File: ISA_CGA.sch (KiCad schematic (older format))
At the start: 0 parts

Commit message: Complete a sheet
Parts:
- added U13: 74LS08, Package_DIP:DIP-14_W7.62mm_LongPads, symbol 74xx:74LS08
- added U14: 74LS32, Package_DIP:DIP-14_W7.62mm_LongPads, symbol 74xx:74LS32
- added U28: 74LS10, Package_DIP:DIP-14_W7.62mm_LongPads, symbol 74xx:74LS10
- added U48: 74LS51, Package_DIP:DIP-14_W7.62mm_LongPads, symbol 74xx:74LS51
- added U49: 74LS02, symbol 74xx:74LS02
- added U62: 74LS125, Package_DIP:DIP-14_W10.16mm_LongPads, symbol 74xx:74LS125
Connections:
- new net GND: U13.14 (VCC), U14.14 (VCC), U28.7 (GND), U48.7 (GND), U49.7 (GND), U62.7 (GND)
- new net VCC: U13.7 (GND), U14.7 (GND), U28.14 (VCC), U48.14 (VCC), U49.14 (VCC), U62.14 (VCC)
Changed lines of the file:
@@
 F1 "CGA_6_6.sch" 50
 $EndSheet
+$Comp
+L 74xx:74LS51 U?
+U 3 1 604901DC
+P 3000 4850
+AR Path="/60463BAE/604901DC" Ref="U?"  Part="1"
+AR Path="/604901DC" Ref="U48"  Part="3"
+F 0 "U48" H 2850 5200 50  0000 C CNN
+F 1 "74LS51" H 3150 5200 50  0000 C CNN
+F 2 "Package_DIP:DIP-14_W7.62mm_LongPads" H 3000 4850 50  0001 C CNN
+F 3 "http://www.ti.com/lit/ds/symlink/sn74ls51.pdf" H 3000 4850 50  0001 C CNN
+	3    3000 4850
+	1    0    0    -1
+$EndComp
+$Comp
+L power:GND #PWR?
+U 1 1 60491E97
+P 3000 5350
+F 0 "#PWR?" H 3000 5100 50  0001 C CNN
+F 1 "GND" H 3005 5177 50  0000 C CNN
+F 2 "" H 3000 5350 50  0001 C CNN
+F 3 "" H 3000 5350 50  0001 C CNN
+	1    3000 5350
+	1    0    0    -1
+$EndComp
+$Comp
+L power:VCC #PWR?
+U 1 1 604924E0
+P 3000 4350
+F 0 "#PWR?" H 3000 4200 50  0001 C CNN
+F 1 "VCC" H 3015 4523 50  0000 C CNN
+F 2 "" H 3000 4350 50  0001 C CNN
+F 3 "" H 3000 4350 50  0001 C CNN
+	1    3000 4350
+	1    0    0    -1
+$EndComp
+$Comp
+L 74xx:74LS02 U?
+U 5 1 60495092
+P 3600 4850
+AR Path="/60463BAE/60495092" Ref="U?"  Part="3"
+AR Path="/60495092" Ref="U49"  Part="5"
+F 0 "U49" H 3500 5200 50  0000 C CNN
+F 1 "74LS02" H 3750 5200 50  0000 C CNN
+F 2 "" H 3600 4850 50  0001 C CNN
+F 3 "http://www.ti.com/lit/gpn/sn74ls02" H 3600 4850 50  0001 C CNN
+	5    3600 4850
+	1    0    0    -1
+$EndComp
+Connection ~ 3000 4350
+Connection ~ 3000 5350
+$Comp
+L 74xx:74LS125 U?
+U 5 1 6049EC67
+P 4200 4850
+AR Path="/60463BAE/6049EC67" Ref="U?"  Part="1"
+AR Path="/6049EC67" Ref="U62"  Part="5"
+F 0 "U62" H 4050 5200 50  0000 C CNN
+F 1 "74LS125" H 4400 5200 50  0000 C CNN
+F 2 "Package_DIP:DIP-14_W10.16mm_LongPads" H 4200 4850 50  0001 C CNN
+F 3 "http://www.ti.com/lit/gpn/sn74LS125" H 4200 4850 50  0001 C CNN
+	5    4200 4850
+	1    0    0    -1
+$EndComp
+Connection ~ 3600 4350
+Connection ~ 3600 5350
+Wire Wire Line
+	3000 4350 3600 4350
+Wire Wire Line
+	3000 5350 3600 5350
+Wire Wire Line
+	3600 4350 4200 4350
+Wire Wire Line
+	3600 5350 4200 5350
+$Comp
+L 74xx:74LS08 U?
+U 5 1 60735FFE
+P 1200 4850
+AR Path="/60463BAE/60735FFE" Ref="U?"  Part="4"
+AR Path="/60735FFE" Ref="U13"  Part="5"
+F 0 "U13" H 1150 4500 50  0000 R CNN
+F 1 "74LS08" H 1500 4500 50  0000 R CNN
+F 2 "Package_DIP:DIP-14_W7.62mm_LongPads" H 1200 4850 50  0001 C CNN
+F 3 "http://www.ti.com/lit/gpn/sn74LS08" H 1200 4850 50  0001 C CNN
+	5    1200 4850
+	1    0    0    1
+$EndComp
+$Comp
+L 74xx:74LS10 U?
+U 4 1 6073B547
+P 2400 4850
+AR Path="/60463BAE/6073B547" Ref="U?"  Part="3"
+AR Path="/6073B547" Ref="U28"  Part="4"
+F 0 "U28" H 2150 5200 50  0000 L CNN
+F 1 "74LS10" H 2450 5200 50  0000 L CNN
+F 2 "Package_DIP:DIP-14_W7.62mm_LongPads" H 2400 4850 50  0001 C CNN
+F 3 "http://www.ti.com/lit/gpn/sn74LS10" H 2400 4850 50  0001 C CNN
+	4    2400 4850
+	1    0    0    -1
+$EndComp
+$Comp
+L 74xx:74LS32 U?
+U 5 1 607513C2
+P 1800 4850
+AR Path="/60463BAE/607513C2" Ref="U?"  Part="2"
+AR Path="/607513C2" Ref="U14"  Part="5"
+F 0 "U14" H 1750 4500 50  0000 R CNN
+F 1 "74LS32" H 2100 4500 50  0000 R CNN
+F 2 "Package_DIP:DIP-14_W7.62mm_LongPads" H 1800 4850 50  0001 C CNN
+F 3 "http://www.ti.com/lit/gpn/sn74LS32" H 1800 4850 50  0001 C CNN
+	5    1800 4850
+	1    0    0    1
+$EndComp
+Wire Wire Line
+	3000 4350 2400 4350
+Connection ~ 1800 4350
+Wire Wire Line
+	1800 4350 1200 4350
+Connection ~ 2400 4350
+Wire Wire Line
+	2400 4350 1800 4350
+Wire Wire Line
+	1200 5350 1800 5350
+Connection ~ 1800 5350
+Wire Wire Line
+	1800 5350 2400 5350
+Connection ~ 2400 5350
+Wire Wire Line
+	2400 5350 3000 5350
 $EndSCHEMATC

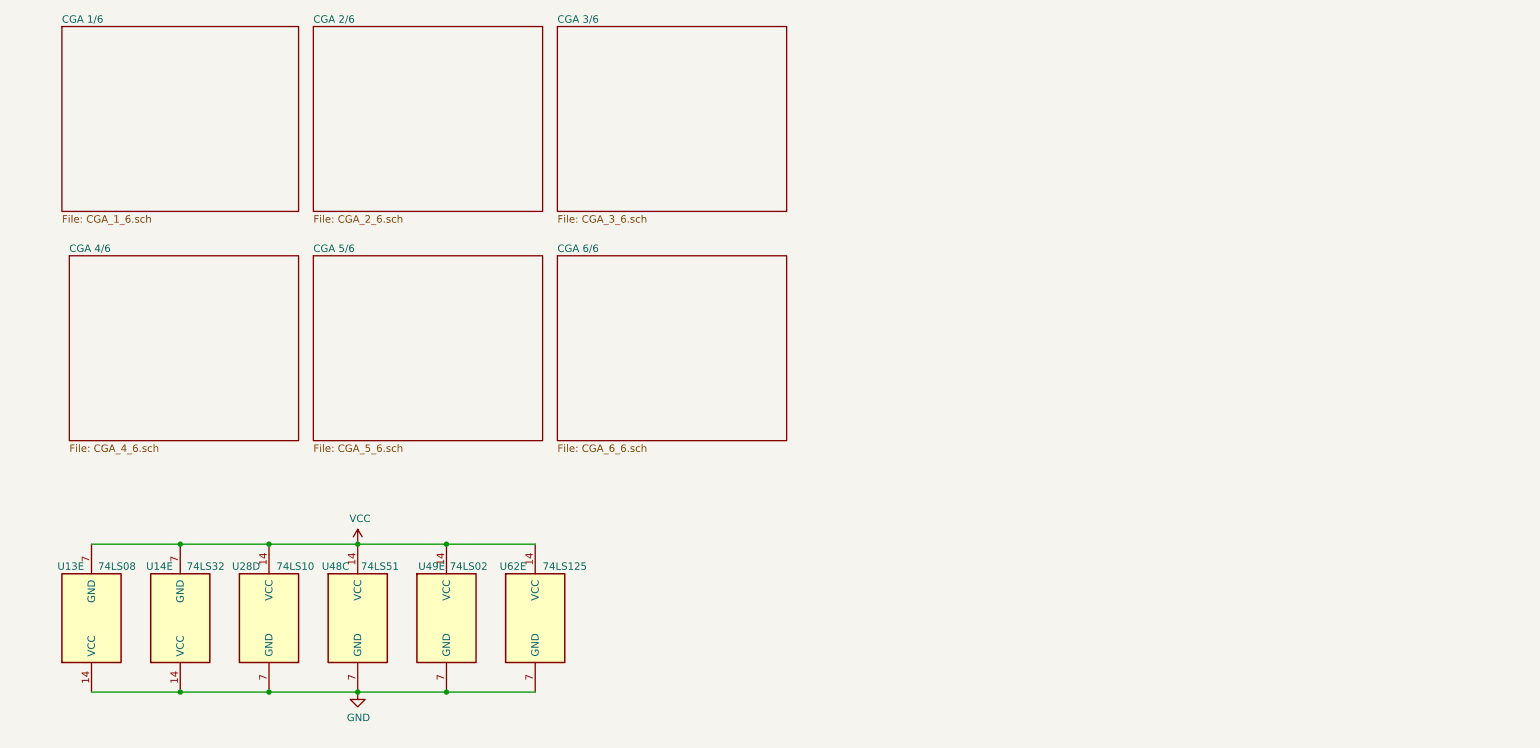
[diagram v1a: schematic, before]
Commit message: Added power for ICs in sheet 2
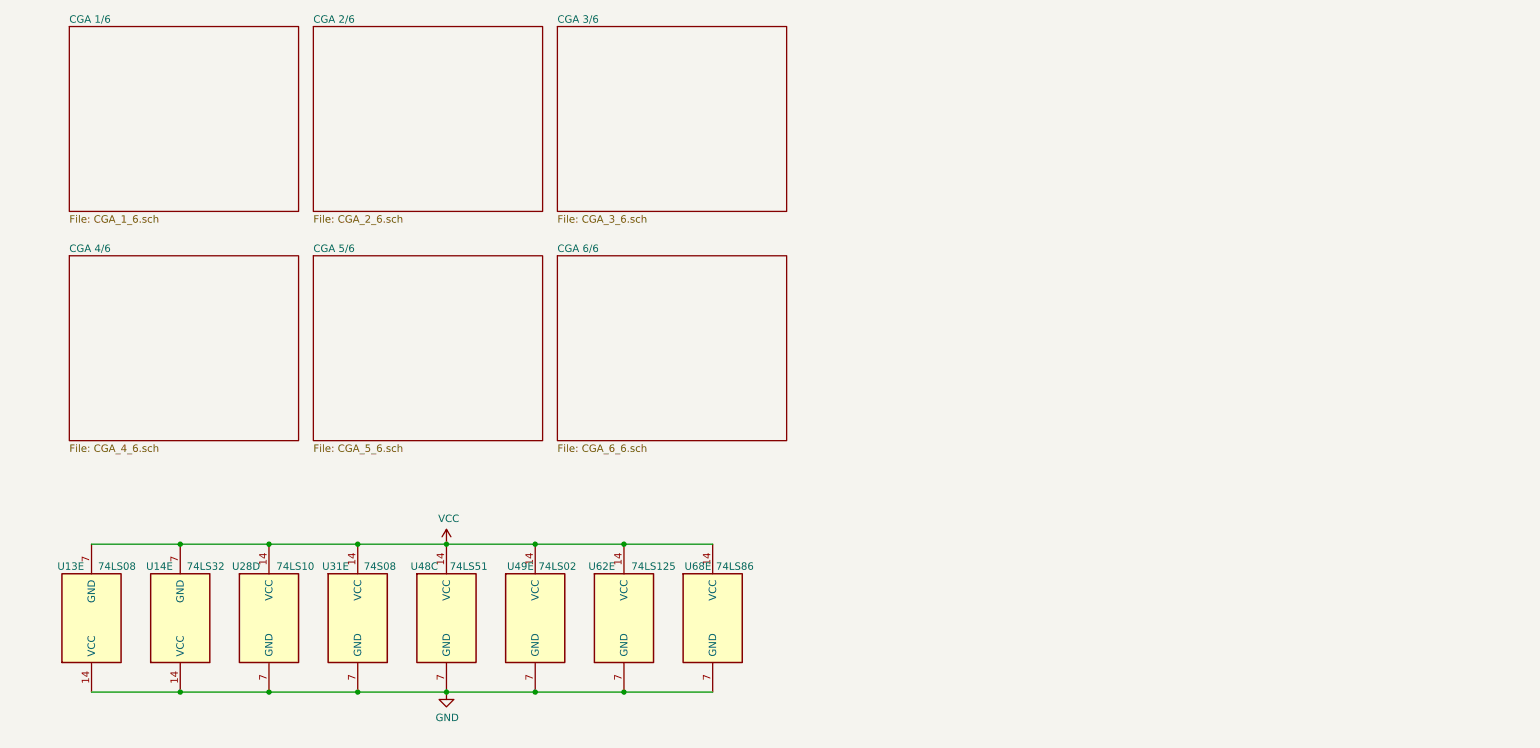
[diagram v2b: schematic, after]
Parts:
- added U31: 74S08, Package_DIP:DIP-14_W7.62mm_LongPads, symbol 74xx:74LS08
- added U68: 74LS86, Package_DIP:DIP-14_W7.62mm_LongPads, symbol 74xx:74LS86
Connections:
- net GND: now also U31.7 (GND), U68.7 (GND)
- net VCC: now also U31.14 (VCC), U68.14 (VCC)
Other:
- moved on the sheet: U48C, U49E, U62E
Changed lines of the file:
@@
 $EndDescr
 $Sheet
-S 1000 850  1600 1250
+S 1050 850  1550 1250
 U 60463BAE
 F0 "CGA 1/6" 50
@@
 L 74xx:74LS51 U?
 U 3 1 604901DC
-P 3000 4850
+P 3600 4850
 AR Path="/60463BAE/604901DC" Ref="U?"  Part="1"
 AR Path="/604901DC" Ref="U48"  Part="3"
-F 0 "U48" H 2850 5200 50  0000 C CNN
-F 1 "74LS51" H 3150 5200 50  0000 C CNN
-F 2 "Package_DIP:DIP-14_W7.62mm_LongPads" H 3000 4850 50  0001 C CNN
-F 3 "http://www.ti.com/lit/ds/symlink/sn74ls51.pdf" H 3000 4850 50  0001 C CNN
-	3    3000 4850
+F 0 "U48" H 3450 5200 50  0000 C CNN
+F 1 "74LS51" H 3750 5200 50  0000 C CNN
+F 2 "Package_DIP:DIP-14_W7.62mm_LongPads" H 3600 4850 50  0001 C CNN
+F 3 "http://www.ti.com/lit/ds/symlink/sn74ls51.pdf" H 3600 4850 50  0001 C CNN
+	3    3600 4850
 	1    0    0    -1
 $EndComp
@@
 L power:GND #PWR?
 U 1 1 60491E97
-P 3000 5350
-F 0 "#PWR?" H 3000 5100 50  0001 C CNN
-F 1 "GND" H 3005 5177 50  0000 C CNN
-F 2 "" H 3000 5350 50  0001 C CNN
-F 3 "" H 3000 5350 50  0001 C CNN
-	1    3000 5350
+P 3600 5350
+F 0 "#PWR?" H 3600 5100 50  0001 C CNN
+F 1 "GND" H 3605 5177 50  0000 C CNN
+F 2 "" H 3600 5350 50  0001 C CNN
+F 3 "" H 3600 5350 50  0001 C CNN
+	1    3600 5350
 	1    0    0    -1
 $EndComp
@@
 L power:VCC #PWR?
 U 1 1 604924E0
-P 3000 4350
-F 0 "#PWR?" H 3000 4200 50  0001 C CNN
-F 1 "VCC" H 3015 4523 50  0000 C CNN
-F 2 "" H 3000 4350 50  0001 C CNN
-F 3 "" H 3000 4350 50  0001 C CNN
-	1    3000 4350
+P 3600 4350
+F 0 "#PWR?" H 3600 4200 50  0001 C CNN
+F 1 "VCC" H 3615 4523 50  0000 C CNN
+F 2 "" H 3600 4350 50  0001 C CNN
+F 3 "" H 3600 4350 50  0001 C CNN
+	1    3600 4350
 	1    0    0    -1
 $EndComp
@@
 L 74xx:74LS02 U?
 U 5 1 60495092
-P 3600 4850
+P 4200 4850
 AR Path="/60463BAE/60495092" Ref="U?"  Part="3"
 AR Path="/60495092" Ref="U49"  Part="5"
-F 0 "U49" H 3500 5200 50  0000 C CNN
-F 1 "74LS02" H 3750 5200 50  0000 C CNN
-F 2 "" H 3600 4850 50  0001 C CNN
-F 3 "http://www.ti.com/lit/gpn/sn74ls02" H 3600 4850 50  0001 C CNN
-	5    3600 4850
-	1    0    0    -1
-$EndComp
-Connection ~ 3000 4350
-Connection ~ 3000 5350
+F 0 "U49" H 4100 5200 50  0000 C CNN
+F 1 "74LS02" H 4350 5200 50  0000 C CNN
+F 2 "" H 4200 4850 50  0001 C CNN
+F 3 "http://www.ti.com/lit/gpn/sn74ls02" H 4200 4850 50  0001 C CNN
+	5    4200 4850
+	1    0    0    -1
+$EndComp
+Connection ~ 3600 4350
+Connection ~ 3600 5350
 $Comp
 L 74xx:74LS125 U?
 U 5 1 6049EC67
-P 4200 4850
+P 4800 4850
 AR Path="/60463BAE/6049EC67" Ref="U?"  Part="1"
 AR Path="/6049EC67" Ref="U62"  Part="5"
-F 0 "U62" H 4050 5200 50  0000 C CNN
-F 1 "74LS125" H 4400 5200 50  0000 C CNN
-F 2 "Package_DIP:DIP-14_W10.16mm_LongPads" H 4200 4850 50  0001 C CNN
-F 3 "http://www.ti.com/lit/gpn/sn74LS125" H 4200 4850 50  0001 C CNN
-	5    4200 4850
-	1    0    0    -1
-$EndComp
-Connection ~ 3600 4350
-Connection ~ 3600 5350
-Wire Wire Line
-	3000 4350 3600 4350
-Wire Wire Line
-	3000 5350 3600 5350
+F 0 "U62" H 4650 5200 50  0000 C CNN
+F 1 "74LS125" H 5000 5200 50  0000 C CNN
+F 2 "Package_DIP:DIP-14_W10.16mm_LongPads" H 4800 4850 50  0001 C CNN
+F 3 "http://www.ti.com/lit/gpn/sn74LS125" H 4800 4850 50  0001 C CNN
+	5    4800 4850
+	1    0    0    -1
+$EndComp
+Connection ~ 4200 4350
+Connection ~ 4200 5350
 Wire Wire Line
 	3600 4350 4200 4350
 Wire Wire Line
 	3600 5350 4200 5350
+Wire Wire Line
+	4200 4350 4800 4350
+Wire Wire Line
+	4200 5350 4800 5350
 $Comp
 L 74xx:74LS08 U?
@@
 $EndComp
 Wire Wire Line
-	3000 4350 2400 4350
+	3600 4350 3000 4350
 Connection ~ 1800 4350
 Wire Wire Line
 	1800 4350 1200 4350
-Connection ~ 2400 4350
 Wire Wire Line
 	2400 4350 1800 4350
@@
 Wire Wire Line
 	1800 5350 2400 5350
+Wire Wire Line
+	3000 5350 3600 5350
+$Comp
+L 74xx:74LS86 U?
+U 5 1 61CD3D2F
+P 5400 4850
+AR Path="/60463C10/61CD3D2F" Ref="U?"  Part="4"
+AR Path="/61CD3D2F" Ref="U68"  Part="5"
+F 0 "U68" H 5300 5200 50  0000 C CNN
+F 1 "74LS86" H 5550 5200 50  0000 C CNN
+F 2 "Package_DIP:DIP-14_W7.62mm_LongPads" H 5400 4850 50  0001 C CNN
+F 3 "74xx/74ls86.pdf" H 5400 4850 50  0001 C CNN
+	5    5400 4850
+	1    0    0    -1
+$EndComp
+Wire Wire Line
+	4800 4350 5400 4350
+Connection ~ 4800 4350
+Wire Wire Line
+	4800 5350 5400 5350
+Connection ~ 4800 5350
+$Comp
+L 74xx:74LS08 U?
+U 5 1 61D13A76
+P 3000 4850
+AR Path="/60463C10/61D13A76" Ref="U?"  Part="3"
+AR Path="/61D13A76" Ref="U31"  Part="5"
+F 0 "U31" H 2850 5200 50  0000 C CNN
+F 1 "74S08" H 3150 5200 50  0000 C CNN
+F 2 "Package_DIP:DIP-14_W7.62mm_LongPads" H 3000 4850 50  0001 C CNN
+F 3 "http://www.ti.com/lit/gpn/sn74LS08" H 3000 4850 50  0001 C CNN
+	5    3000 4850
+	1    0    0    -1
+$EndComp
+Wire Wire Line
+	3000 4350 2400 4350
+Connection ~ 3000 4350
+Connection ~ 2400 4350
+Wire Wire Line
+	3000 5350 2400 5350
+Connection ~ 3000 5350
 Connection ~ 2400 5350
-Wire Wire Line
-	2400 5350 3000 5350
 $EndSCHEMATC

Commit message: Begin drawing sheet 3/6
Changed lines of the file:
@@
 $EndSheet
 $Sheet
-S 1050 2400 1550 1250
+S 6050 850  1550 1250
 U 60463CC5
 F0 "CGA 4/6" 50
@@
 $EndSheet
 $Sheet
-S 2700 2400 1550 1250
+S 7700 850  1550 1250
 U 60463CF3
 F0 "CGA 5/6" 50
@@
 $EndSheet
 $Sheet
-S 4350 2400 1550 1250
+S 9350 850  1550 1250
 U 60463D9E
 F0 "CGA 6/6" 50

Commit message: More sheet 3
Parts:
- added U1: 74S112, Package_DIP:DIP-16_W7.62mm_LongPads, symbol 74xx:74LS112
- added U12: 74LS393, Package_DIP:DIP-14_W7.62mm_LongPads, symbol 74xx:74LS393
- added U29: 74S04, Package_DIP:DIP-14_W7.62mm_LongPads, symbol 74xx:74LS04
- added U3: 74S86, Package_DIP:DIP-14_W7.62mm_LongPads, symbol 74xx:74LS86
- added U30: 74LS32, symbol 74xx:74LS32
- added U42: 74LS86, Package_DIP:DIP-14_W7.62mm_LongPads, symbol 74xx:74LS86
- added U6: 74LS04, Package_DIP:DIP-14_W7.62mm_LongPads, symbol 74xx:74LS04
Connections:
- removed net GND: U13.14 (VCC), U14.14 (VCC), U28.7 (GND), U31.7 (GND), U48.7 (GND), U49.7 (GND), U62.7 (GND), U68.7 (GND)
- removed net VCC: U13.7 (GND), U14.7 (GND), U28.14 (VCC), U31.14 (VCC), U48.14 (VCC), U49.14 (VCC), U62.14 (VCC), U68.14 (VCC)
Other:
- moved on the sheet: U13E, U14E, U28D, U31E, U48C, U49E, U62E, U68E
